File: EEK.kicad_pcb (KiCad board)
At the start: 2 copper layers, 165 x 51.8 mm, 52 parts, among them J1 Screw_Terminal_01x02

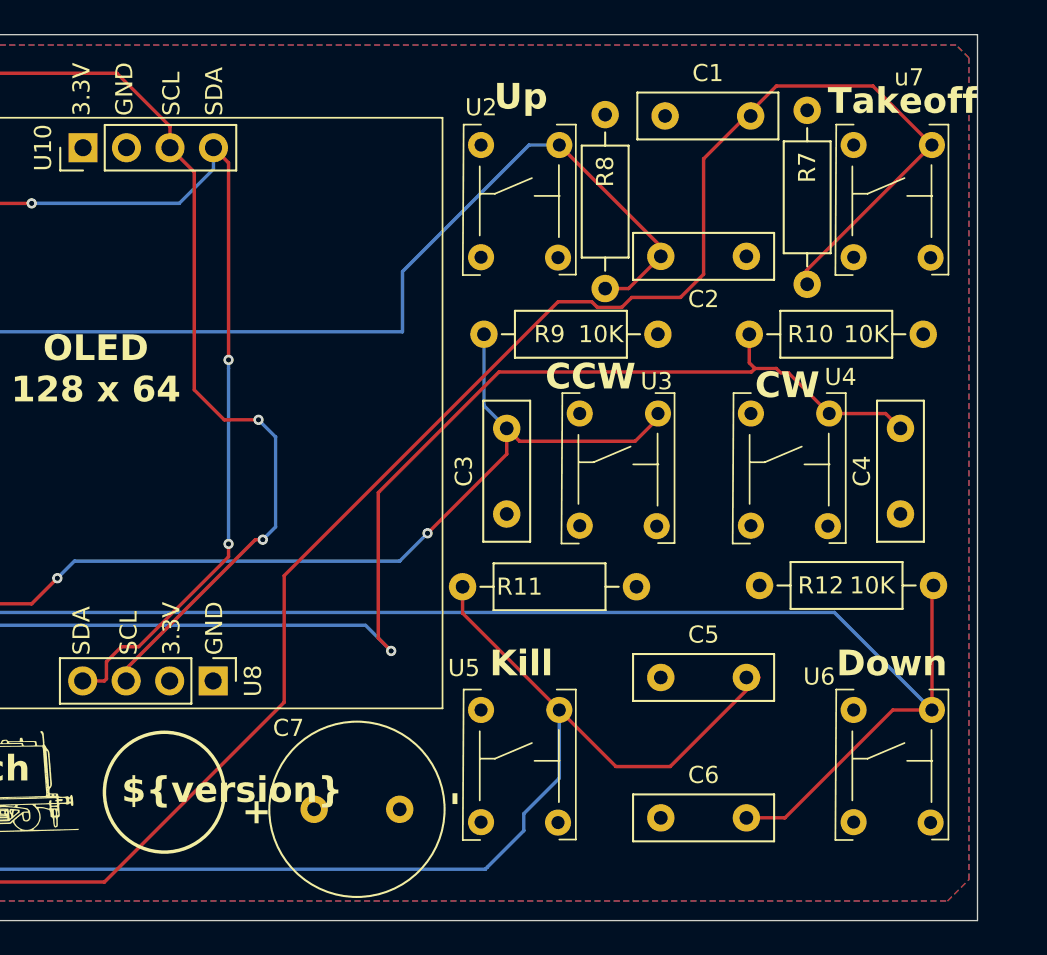
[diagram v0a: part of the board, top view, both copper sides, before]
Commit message: Invert Takeoff and Up switches
Invert Takeoff and Up switches
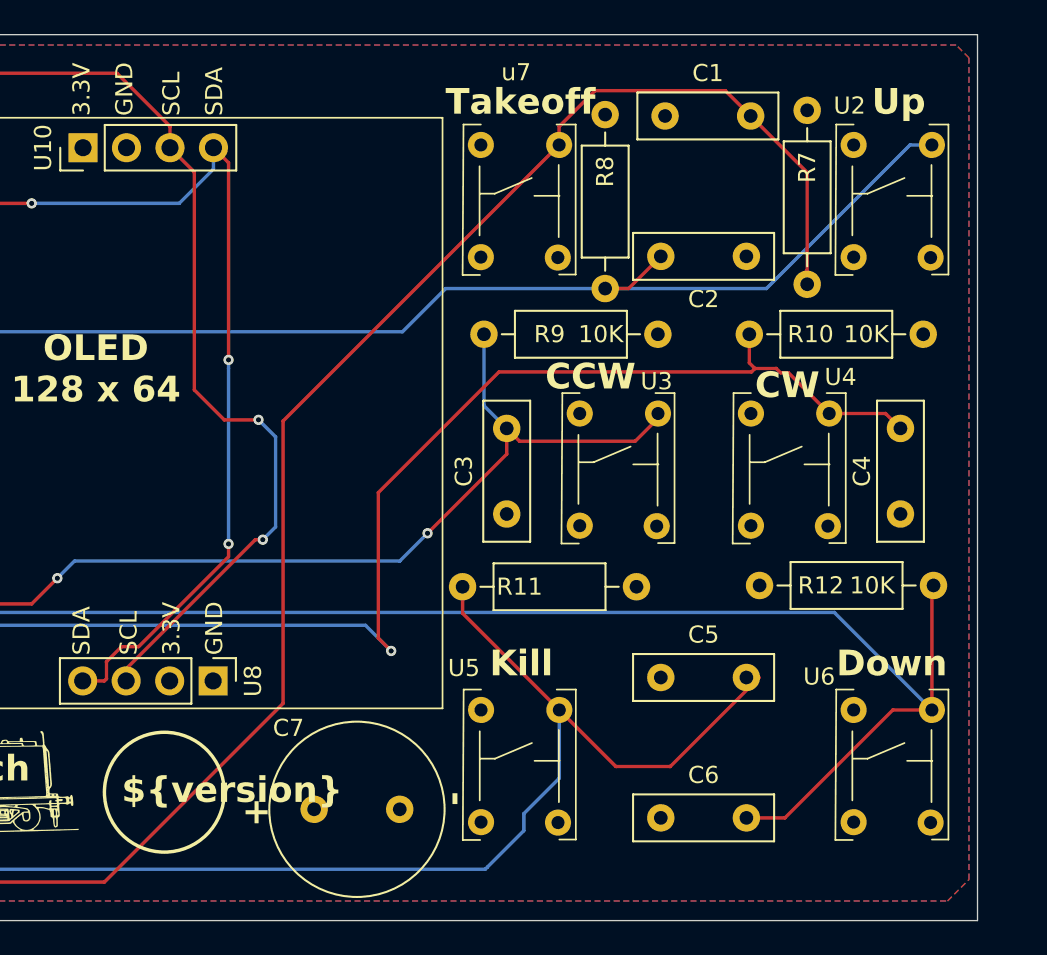
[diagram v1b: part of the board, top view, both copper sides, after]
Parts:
- moved u7 21.8 mm to (183.6, 78.1)
- moved U2 21.8 mm to (205.3, 78.1)
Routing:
- net /Up: track 137.5 -> 148.8 mm
- net /Takeoff: track 203.4 -> 194.4 mm
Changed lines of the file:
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@@
 	(footprint "PH_lib:SW_Tactile"
 		(layer "F.Cu")
-		(at 183.58 78.1168)
+		(at 205.3448 78.1127)
 		(property "Reference" "U2"
-			(at -5.08 2.8832 0)
+			(at -5.3198 2.7873 0)
 			(unlocked yes)
 			(layer "F.SilkS")
@@
 	(footprint "PH_lib:SW_Tactile"
 		(layer "F.Cu")
-		(at 205.3448 78.1168)
+		(at 183.5698 78.1127)
 		(property "Reference" "u7"
-			(at -1.8448 1.1332 0)
+			(at -3.0198 0.8373 0)
 			(unlocked yes)
 			(layer "F.SilkS")
@@
 			(unlocked yes)
 			(layer "F.Fab")
+			(hide yes)
 			(effects
 				(font
@@
 	)
 	(gr_text "Up"
-		(at 179.25 81.25 0)
+		(at 201.325 81.55 0)
 		(layer "F.SilkS")
 		(effects
@@
 	)
 	(gr_text "Takeoff"
-		(at 198.75 81.5 0)
+		(at 176.425 81.55 0)
 		(layer "F.SilkS")
 		(effects
@@
 	)
 	(segment
-		(start 183.072 83.1968)
-		(end 189 89.1248)
+		(start 189 89.1248)
+		(end 189 89.7)
 		(width 0.2)
 		(layer "F.Cu")
@@
 	)
 	(segment
-		(start 189 89.1248)
-		(end 189 89.7)
+		(start 173.9107 94.1041)
+		(end 176.4348 91.58)
 		(width 0.2)
-		(layer "F.Cu")
+		(layer "B.Cu")
 		(net 20)
 	)
@@
 	)
 	(segment
-		(start 173.9107 90.5893)
-		(end 181.3032 83.1968)
-		(width 0.2)
-		(layer "B.Cu")
-		(net 20)
-	)
-	(segment
 		(start 125.487258 94.1041)
 		(end 173.9107 94.1041)
@@
 	)
 	(segment
-		(start 173.9107 94.1041)
-		(end 173.9107 90.5893)
-		(width 0.2)
-		(layer "B.Cu")
-		(net 20)
-	)
-	(segment
-		(start 181.3032 83.1968)
-		(end 183.072 83.1968)
+		(start 195.17 91.58)
+		(end 203.5573 83.1927)
 		(width 0.2)
 		(layer "B.Cu")
@@
 	)
 	(segment
-		(start 185.294365 92.68)
-		(end 186.72 92.68)
+		(start 203.5573 83.1927)
+		(end 204.8368 83.1927)
 		(width 0.2)
-		(layer "F.Cu")
-		(net 21)
+		(layer "B.Cu")
+		(net 20)
 	)
 	(segment
-		(start 183.0041 92.35)
-		(end 184.964365 92.35)
+		(start 185.75 91.58)
+		(end 195.17 91.58)
 		(width 0.2)
-		(layer "F.Cu")
-		(net 21)
+		(layer "B.Cu")
+		(net 20)
 	)
 	(segment
-		(start 51.4175 118.713085)
-		(end 54.375 121.670584)
+		(start 176.4348 91.58)
+		(end 185.75 91.58)
 		(width 0.2)
-		(layer "F.Cu")
-		(net 21)
+		(layer "B.Cu")
+		(net 20)
 	)
 	(segment
-		(start 191.5 90.75)
-		(end 191.5 84)
+		(start 51.4175 118.713085)
+		(end 54.375 121.670584)
 		(width 0.2)
 		(layer "F.Cu")
@@
 	)
 	(segment
-		(start 195.75 79.75)
-		(end 201.39 79.75)
+		(start 183.0618 82.11507)
+		(end 185.15687 80.02)
 		(width 0.2)
 		(layer "F.Cu")
@@
 	)
 	(segment
-		(start 184.964365 92.35)
-		(end 185.294365 92.68)
+		(start 183.0618 83.1927)
+		(end 183.0618 82.11507)
 		(width 0.2)
 		(layer "F.Cu")
@@
 	)
 	(segment
-		(start 186.72 92.68)
-		(end 187.3 92.1)
+		(start 185.15687 80.02)
+		(end 192.77 80.02)
 		(width 0.2)
 		(layer "F.Cu")
@@
 	)
 	(segment
-		(start 191.5 84)
-		(end 195.75 79.75)
-		(width 0.2)
-		(layer "F.Cu")
-		(net 21)
-	)
-	(segment
-		(start 167 108.3541)
-		(end 183.0041 92.35)
-		(width 0.2)
-		(layer "F.Cu")
-		(net 21)
-	)
-	(segment
-		(start 187.3 92.1)
-		(end 190.15 92.1)
+		(start 197.55 84.8)
+		(end 197.55 91.33)
 		(width 0.2)
 		(layer "F.Cu")
@@
 	)
 	(segment
-		(start 201.39 79.75)
-		(end 204.8368 83.1968)
+		(start 192.77 80.02)
+		(end 194.25 81.5)
 		(width 0.2)
 		(layer "F.Cu")
@@
 	)
 	(segment
-		(start 167 115.75)
-		(end 167 108.3541)
+		(start 166.9375 115.8125)
+		(end 166.9375 99.317)
 		(width 0.2)
 		(layer "F.Cu")
@@
 	)
 	(segment
-		(start 156.5 126.25)
-		(end 167 115.75)
+		(start 54.375 124.625)
+		(end 56 126.25)
 		(width 0.2)
 		(layer "F.Cu")
@@
 	)
 	(segment
-		(start 54.375 124.625)
-		(end 56 126.25)
+		(start 194.25 81.5)
+		(end 197.55 84.8)
 		(width 0.2)
 		(layer "F.Cu")
@@
 	)
 	(segment
-		(start 190.15 92.1)
-		(end 191.5 90.75)
+		(start 166.9375 99.317)
+		(end 183.0618 83.1927)
 		(width 0.2)
 		(layer "F.Cu")
@@
 	)
 	(segment
-		(start 197.5 90.5336)
-		(end 204.8368 83.1968)
+		(start 156.5 126.25)
+		(end 166.9375 115.8125)
 		(width 0.2)
 		(layer "F.Cu")

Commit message: gerber files V1.1 and QR code on silkscreen
gerber files V1.1 and QR code on silkscreen
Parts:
- added QR1: githubEEK, PH_lib:githubEEK, B.Cu at (157.3, 97.4)
- renumbered G*** to G001
